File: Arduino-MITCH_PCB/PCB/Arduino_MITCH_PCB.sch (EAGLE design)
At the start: 9 parts, among them IC1 TC58CVG2S0HRAIJ, J1 1725656

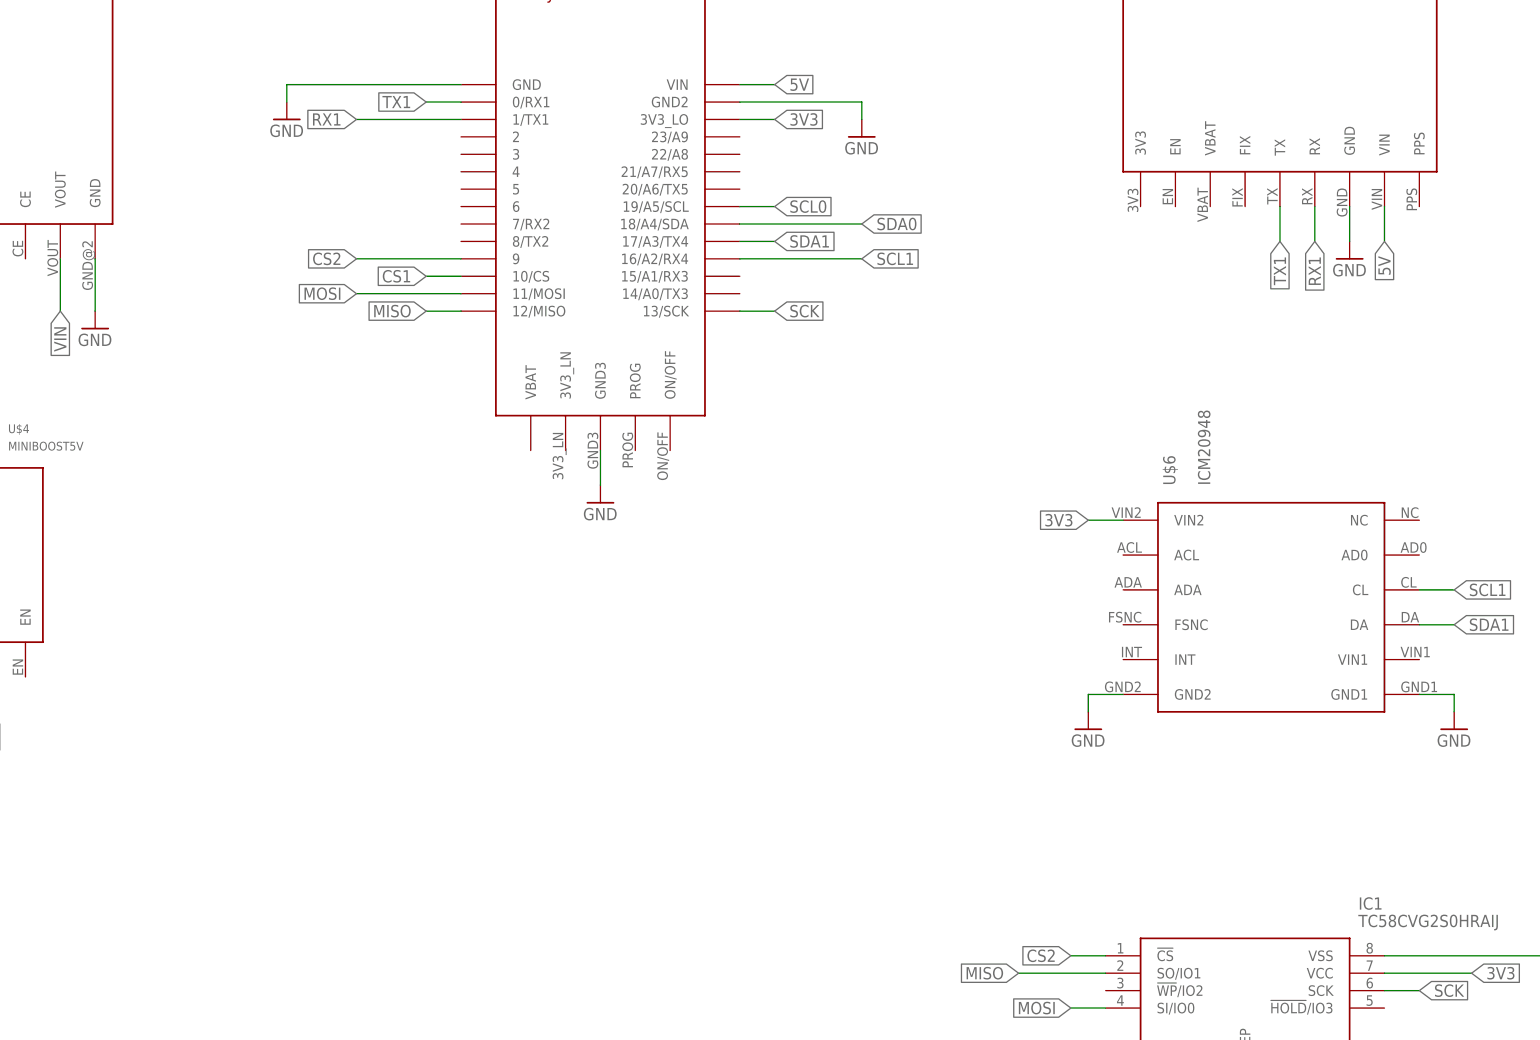
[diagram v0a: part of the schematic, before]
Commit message: Added a piezo buzzer to PCB
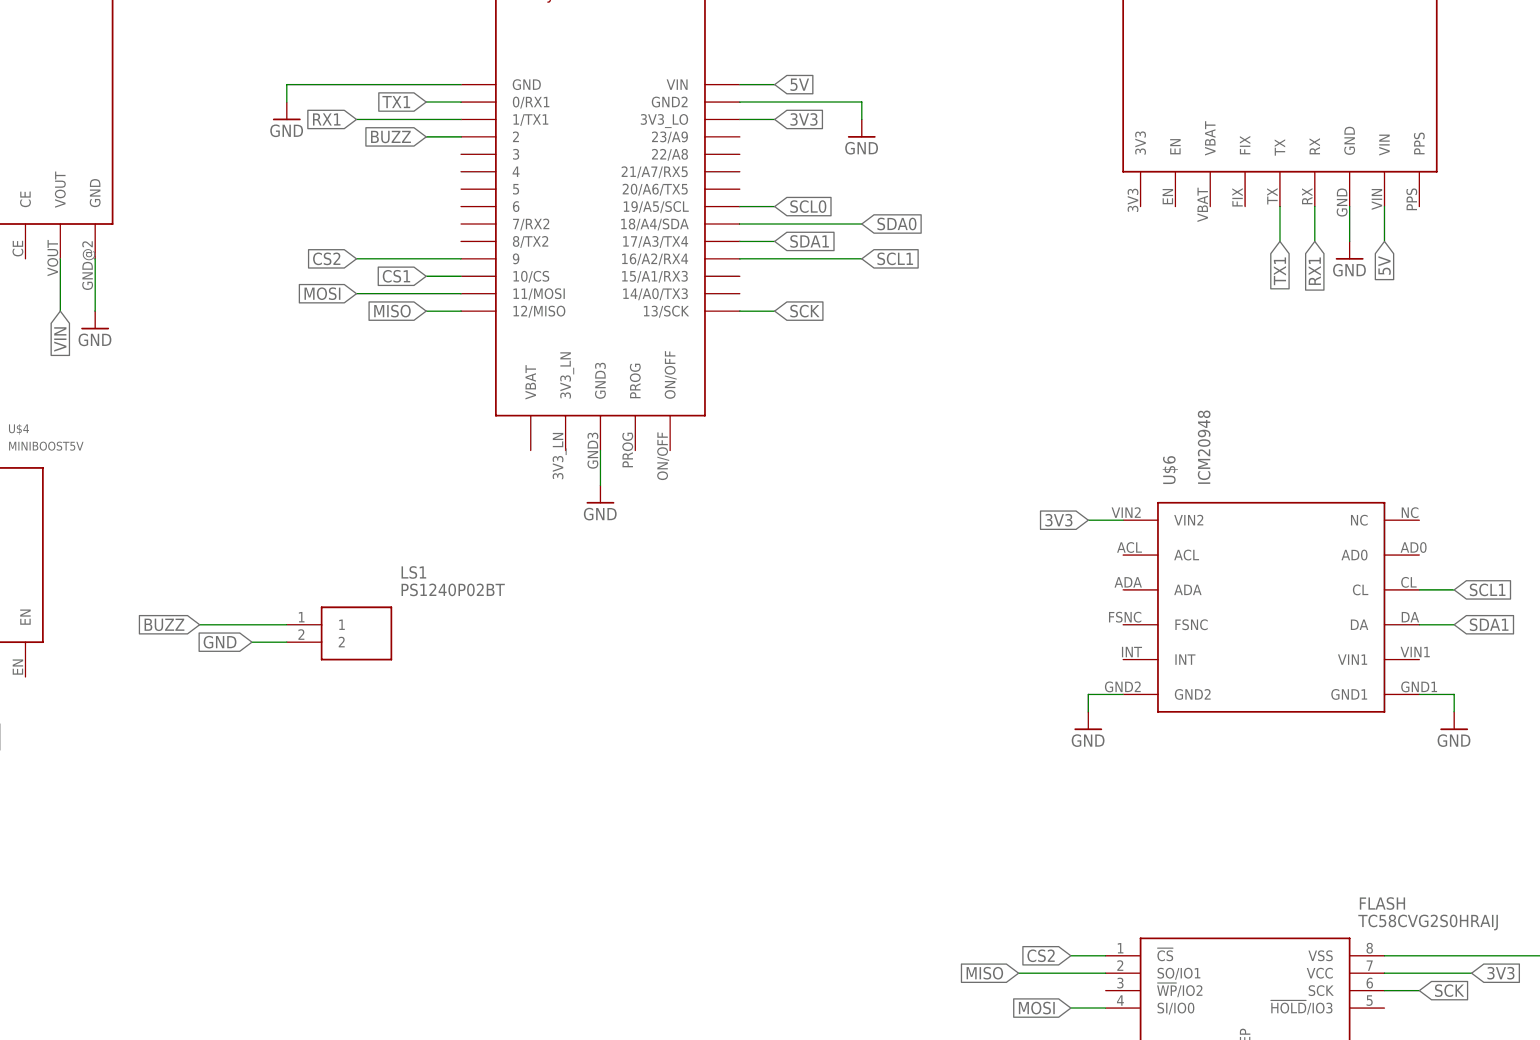
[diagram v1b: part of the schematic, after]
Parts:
- added LS1: PS1240P02BT, SamacSys_Parts:PS1240P02BT
- renumbered IC1 to FLASH
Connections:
- new net BUZZ: LS1.1, U$1.2
- net GND: now also LS1.2
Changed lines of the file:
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@@
 <part name="U$1" library="Arduino-MITCH_Breakouts" deviceset="TEENSY_4.0-BASIC" device=""/>
 <part name="U$2" library="Arduino-MITCH_Breakouts" deviceset="ULTIMATE_GPS" device=""/>
-<part name="IC1" library="Arduino-MITCH_Breakouts" deviceset="TC58CVG2S0HRAIJ" device=""/>
+<part name="FLASH" library="Arduino-MITCH_Breakouts" deviceset="TC58CVG2S0HRAIJ" device=""/>
 <part name="U$3" library="Arduino-MITCH_Breakouts" deviceset="SPARKFUN-BATTERY-BABYSITTER" device=""/>
 <part name="U$4" library="Arduino-MITCH_Breakouts" deviceset="MINIBOOST5V" device=""/>
@@
 <part name="GND13" library="supply1" library_urn="urn:adsk.eagle:library:371" deviceset="GND" device=""/>
 <part name="GND14" library="supply1" library_urn="urn:adsk.eagle:library:371" deviceset="GND" device=""/>
+<part name="LS1" library="SamacSys_Parts" deviceset="PS1240P02BT" device=""/>
 </parts>
 <sheets>
@@
 <attribute name="VALUE" x="86.36" y="121.92" size="2.54" layer="96"/>
 </instance>
-<instance part="IC1" gate="G$1" x="50.8" y="-22.86" smashed="yes">
+<instance part="FLASH" gate="G$1" x="50.8" y="-22.86" smashed="yes">
 <attribute name="NAME" x="87.63" y="-15.24" size="1.778" layer="95" align="center-left"/>
 <attribute name="VALUE" x="87.63" y="-17.78" size="1.778" layer="96" align="center-left"/>
@@
 <instance part="GND14" gate="1" x="116.84" y="-27.94" smashed="yes">
 <attribute name="VALUE" x="114.3" y="-30.48" size="1.778" layer="96"/>
+</instance>
+<instance part="LS1" gate="G$1" x="-68.58" y="25.4" smashed="yes">
+<attribute name="NAME" x="-52.07" y="33.02" size="1.778" layer="95" align="center-left"/>
+<attribute name="VALUE" x="-52.07" y="30.48" size="1.778" layer="96" align="center-left"/>
 </instance>
 </instances>
@@
 </segment>
 <segment>
-<pinref part="IC1" gate="G$1" pin="VSS"/>
+<pinref part="FLASH" gate="G$1" pin="VSS"/>
 <wire x1="91.44" y1="-22.86" x2="116.84" y2="-22.86" width="0.1524" layer="91"/>
 <wire x1="116.84" y1="-22.86" x2="116.84" y2="-25.4" width="0.1524" layer="91"/>
 <pinref part="GND14" gate="1" pin="GND"/>
+</segment>
+<segment>
+<pinref part="LS1" gate="G$1" pin="2"/>
+<wire x1="-68.58" y1="22.86" x2="-73.66" y2="22.86" width="0.1524" layer="91"/>
+<label x="-73.66" y="22.86" size="1.778" layer="95" rot="R180" xref="yes"/>
 </segment>
 </net>
@@
 </segment>
 <segment>
-<pinref part="IC1" gate="G$1" pin="VCC"/>
+<pinref part="FLASH" gate="G$1" pin="VCC"/>
 <wire x1="91.44" y1="-25.4" x2="104.14" y2="-25.4" width="0.1524" layer="91"/>
 <label x="104.14" y="-25.4" size="1.778" layer="95" xref="yes"/>
@@
 </segment>
 <segment>
-<pinref part="IC1" gate="G$1" pin="SCK"/>
+<pinref part="FLASH" gate="G$1" pin="SCK"/>
 <wire x1="91.44" y1="-27.94" x2="96.52" y2="-27.94" width="0.1524" layer="91"/>
 <label x="96.52" y="-27.94" size="1.778" layer="95" xref="yes"/>
@@
 </segment>
 <segment>
-<pinref part="IC1" gate="G$1" pin="SO/IO1"/>
+<pinref part="FLASH" gate="G$1" pin="SO/IO1"/>
 <wire x1="50.8" y1="-25.4" x2="38.1" y2="-25.4" width="0.1524" layer="91"/>
 <label x="38.1" y="-25.4" size="1.778" layer="95" rot="R180" xref="yes"/>
@@
 </segment>
 <segment>
-<pinref part="IC1" gate="G$1" pin="SI/IO0"/>
+<pinref part="FLASH" gate="G$1" pin="SI/IO0"/>
 <wire x1="50.8" y1="-30.48" x2="45.72" y2="-30.48" width="0.1524" layer="91"/>
 <label x="45.72" y="-30.48" size="1.778" layer="95" rot="R180" xref="yes"/>
@@
 <net name="CS2" class="0">
 <segment>
-<pinref part="IC1" gate="G$1" pin="!CS"/>
+<pinref part="FLASH" gate="G$1" pin="!CS"/>
 <wire x1="50.8" y1="-22.86" x2="45.72" y2="-22.86" width="0.1524" layer="91"/>
 <label x="45.72" y="-22.86" size="1.778" layer="95" rot="R180" xref="yes"/>
@@
 </segment>
 </net>
+<net name="BUZZ" class="0">
+<segment>
+<pinref part="LS1" gate="G$1" pin="1"/>
+<wire x1="-68.58" y1="25.4" x2="-81.28" y2="25.4" width="0.1524" layer="91"/>
+<label x="-81.28" y="25.4" size="1.778" layer="95" rot="R180" xref="yes"/>
+</segment>
+<segment>
+<pinref part="U$1" gate="G$1" pin="2"/>
+<wire x1="-43.18" y1="96.52" x2="-48.26" y2="96.52" width="0.1524" layer="91"/>
+<label x="-48.26" y="96.52" size="1.778" layer="95" rot="R180" xref="yes"/>
+</segment>
+</net>

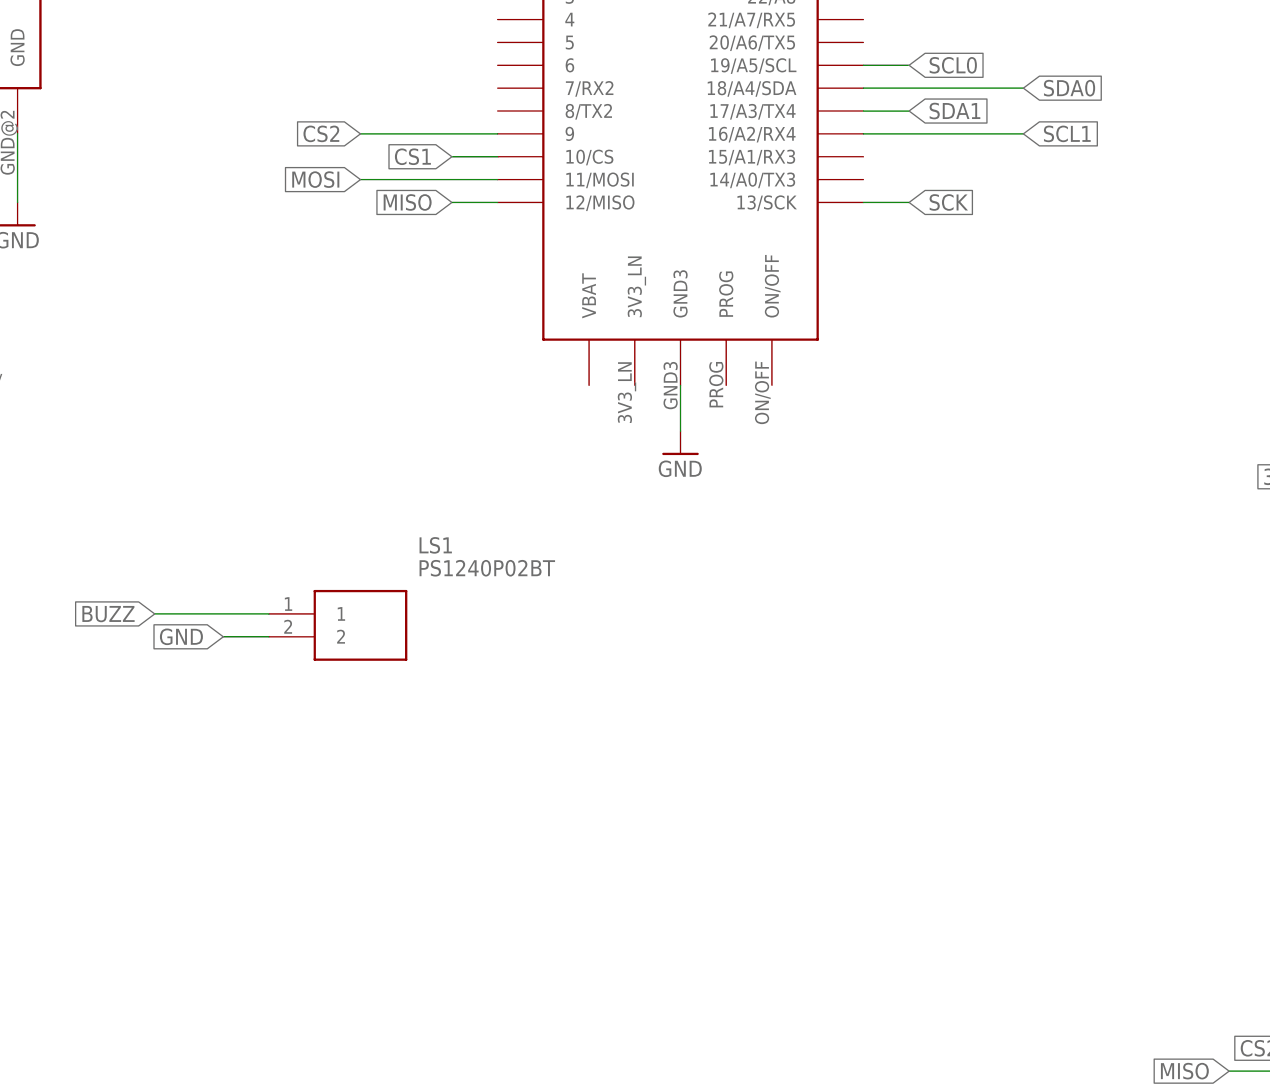
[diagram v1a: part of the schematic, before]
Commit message: Added LED for debugging and custom images
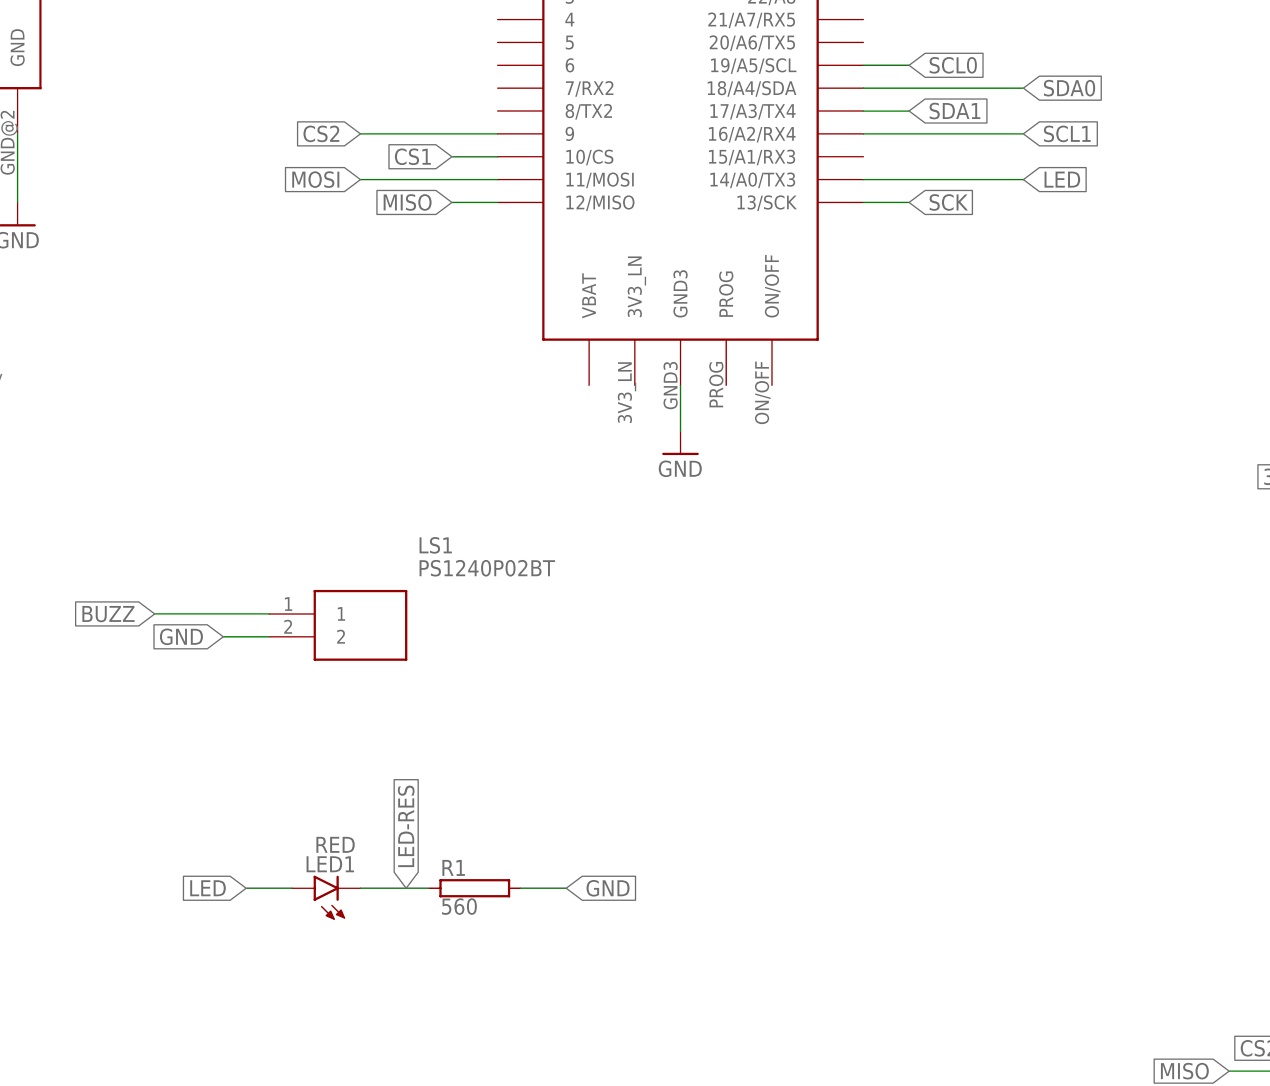
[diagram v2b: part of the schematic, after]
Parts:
- added LED1: RED, led:LED5MM
- added R1: 560, resistor-power:RHPS58
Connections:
- new net LED: LED1.A, U$1.14/A0/TX3
- new net LED-RES: LED1.C, R1.1
- net GND: now also R1.2
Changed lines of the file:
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@@
 <part name="GND14" library="supply1" library_urn="urn:adsk.eagle:library:371" deviceset="GND" device=""/>
 <part name="LS1" library="SamacSys_Parts" deviceset="PS1240P02BT" device=""/>
+<part name="LED1" library="led" library_urn="urn:adsk.eagle:library:259" deviceset="LED" device="5MM" package3d_urn="urn:adsk.eagle:package:15799/2" value="RED"/>
+<part name="R1" library="resistor-power" library_urn="urn:adsk.eagle:library:344" deviceset="R" device="HPS58" package3d_urn="urn:adsk.eagle:package:25160/1" value="560"/>
 </parts>
 <sheets>
@@
 <attribute name="VALUE" x="-52.07" y="30.48" size="1.778" layer="96" align="center-left"/>
 </instance>
+<instance part="LED1" gate="G$1" x="-63.5" y="-5.08" smashed="yes" rot="R90">
+<attribute name="NAME" x="-58.928" y="-1.524" size="1.778" layer="95" rot="R180"/>
+<attribute name="VALUE" x="-58.928" y="0.635" size="1.778" layer="96" rot="R180"/>
+</instance>
+<instance part="R1" gate="G$1" x="-45.72" y="-5.08" smashed="yes">
+<attribute name="NAME" x="-49.53" y="-3.7084" size="1.778" layer="95"/>
+<attribute name="VALUE" x="-49.53" y="-8.001" size="1.778" layer="96"/>
+</instance>
 </instances>
 <busses>
@@
 <label x="-73.66" y="22.86" size="1.778" layer="95" rot="R180" xref="yes"/>
 </segment>
+<segment>
+<pinref part="R1" gate="G$1" pin="2"/>
+<wire x1="-40.64" y1="-5.08" x2="-35.56" y2="-5.08" width="0.1524" layer="91"/>
+<label x="-35.56" y="-5.08" size="1.778" layer="95" xref="yes"/>
+</segment>
 </net>
 <net name="BAT_VIN" class="0">
@@
 <wire x1="-43.18" y1="96.52" x2="-48.26" y2="96.52" width="0.1524" layer="91"/>
 <label x="-48.26" y="96.52" size="1.778" layer="95" rot="R180" xref="yes"/>
+</segment>
+</net>
+<net name="LED-RES" class="0">
+<segment>
+<pinref part="LED1" gate="G$1" pin="C"/>
+<pinref part="R1" gate="G$1" pin="1"/>
+<wire x1="-58.42" y1="-5.08" x2="-50.8" y2="-5.08" width="0.1524" layer="91"/>
+<label x="-53.34" y="-5.08" size="1.778" layer="95" rot="R90" xref="yes"/>
+</segment>
+</net>
+<net name="LED" class="0">
+<segment>
+<pinref part="LED1" gate="G$1" pin="A"/>
+<wire x1="-66.04" y1="-5.08" x2="-71.12" y2="-5.08" width="0.1524" layer="91"/>
+<label x="-71.12" y="-5.08" size="1.778" layer="95" rot="R180" xref="yes"/>
+</segment>
+<segment>
+<pinref part="U$1" gate="G$1" pin="14/A0/TX3"/>
+<wire x1="-2.54" y1="73.66" x2="15.24" y2="73.66" width="0.1524" layer="91"/>
+<label x="15.24" y="73.66" size="1.778" layer="95" xref="yes"/>
 </segment>
 </net>
@@
 will not be understood (or retained) with this version.
 </note>
+<note version="8.3" severity="warning">
+Since Version 8.3, EAGLE supports the association of 3D packages
+with devices in libraries, schematics, and board files. Those 3D
+packages will not be understood (or retained) with this version.
+</note>
 </compatibility>
